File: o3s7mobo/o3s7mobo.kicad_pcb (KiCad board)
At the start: 2 copper layers, 330 x 216 mm, 0 parts

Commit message: Initial placement of 0.1" headers
Obviously far from finalized, but I wanted to start with what I could easily add.
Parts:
- added REF**: PinHeader_2x05_P2.54mm_Vertical, Connector_PinHeader_2.54mm:PinHeader_2x05_P2.54mm_Vertical, F.Cu at (256.0, 201.5)
- added REF**: PinHeader_2x20_P2.54mm_Vertical, Connector_PinHeader_2.54mm:PinHeader_2x20_P2.54mm_Vertical, F.Cu at (254.5, 186.5)
- added REF**: PinHeader_2x05_P2.54mm_Vertical, Connector_PinHeader_2.54mm:PinHeader_2x05_P2.54mm_Vertical, F.Cu at (275.0, 201.5)
- added REF**: PinHeader_2x13_P2.54mm_Vertical, Connector_PinHeader_2.54mm:PinHeader_2x13_P2.54mm_Vertical, F.Cu at (40.0, 37.0)
- added REF**: PinHeader_2x05_P2.54mm_Vertical, Connector_PinHeader_2.54mm:PinHeader_2x05_P2.54mm_Vertical, F.Cu at (60.5, 23.0)
- added REF**: PinHeader_2x05_P2.54mm_Vertical, Connector_PinHeader_2.54mm:PinHeader_2x05_P2.54mm_Vertical, F.Cu at (41.5, 23.0)
- added REF**: PinHeader_2x09_P2.54mm_Vertical, Connector_PinHeader_2.54mm:PinHeader_2x09_P2.54mm_Vertical, F.Cu at (40.5, 50.0)
- added REF**: PinHeader_2x08_P2.54mm_Vertical, Connector_PinHeader_2.54mm:PinHeader_2x08_P2.54mm_Vertical, F.Cu at (294.5, 201.5)
- added REF**: PinHeader_2x17_P2.54mm_Vertical, Connector_PinHeader_2.54mm:PinHeader_2x17_P2.54mm_Vertical, F.Cu at (254.5, 162.0)
- added REF**: PinHeader_2x20_P2.54mm_Vertical, Connector_PinHeader_2.54mm:PinHeader_2x20_P2.54mm_Vertical, F.Cu at (254.5, 176.0)

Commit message: Fix floppy connector, place labels of headers
I still need to finalize the front panel design, but I'm probably going to have something more standard.
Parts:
- removed REF**: PinHeader_2x17_P2.54mm_Vertical, Connector_PinHeader_2.54mm:PinHeader_2x17_P2.54mm_Vertical
- added FD0/1: PinHeader_2x16_P2.54mm_Vertical, Connector_PinHeader_2.54mm:PinHeader_2x16_P2.54mm_Vertical, F.Cu at (255.0, 166.0)
- renumbered REF** to ATXFORM, REF** to FPANEL, REF** to IDE0, REF** to IDE1, REF** to LPT0, REF** to SERIAL0, REF** to SERIAL1, REF** to USB2_0, REF** to USB2_1

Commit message: Removed key pins on headers
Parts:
- removed IDE0: PinHeader_2x20_P2.54mm_Vertical, Connector_PinHeader_2.54mm:PinHeader_2x20_P2.54mm_Vertical
- added IDE2: PinHeader_2x20_P2.54mm_Vertical, Connector_PinHeader_2.54mm:PinHeader_2x20_P2.54mm_Vertical, F.Cu at (255.0, 182.5)
- moved IDE1 13.0 mm to (255.0, 173.5)
- moved FLOPPY 4.61 mm to (256.0, 161.5)
- renumbered FD0/1 to FLOPPY, LPT0 to PARALLEL1, SERIAL0 to SERIAL1, SERIAL1 to SERIAL2

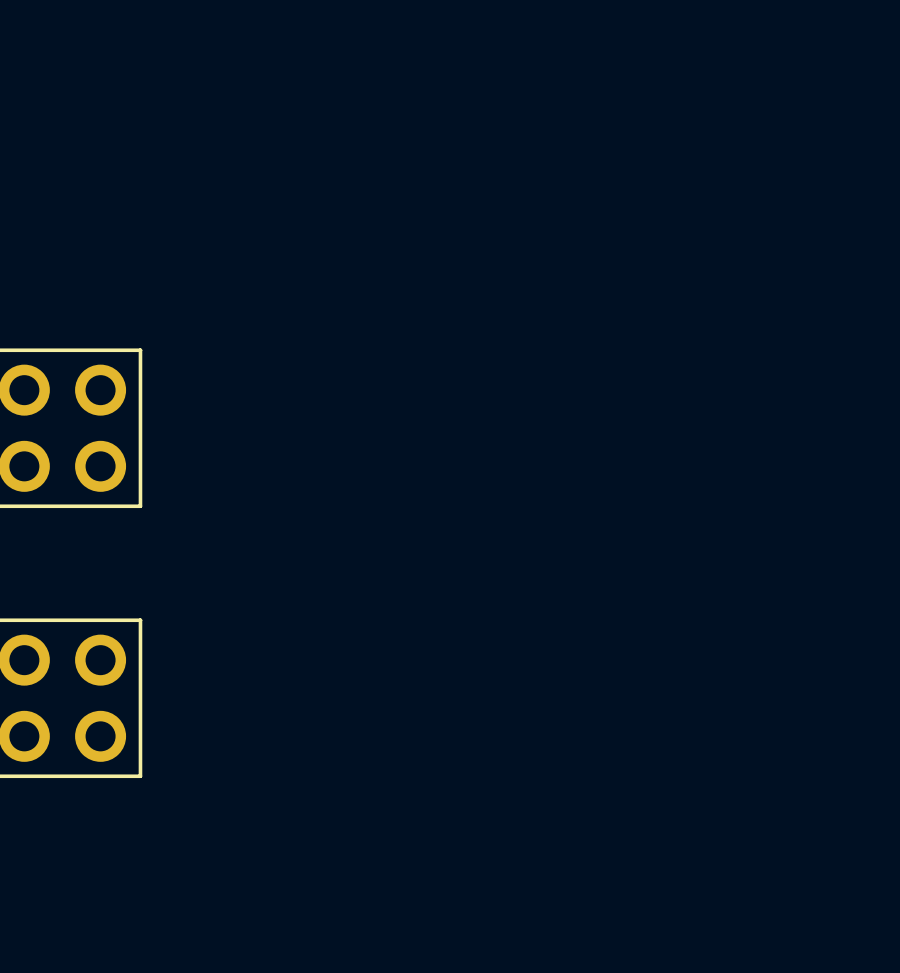
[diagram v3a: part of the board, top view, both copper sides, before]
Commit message: Added CMOS battery socket, minor bugfixing
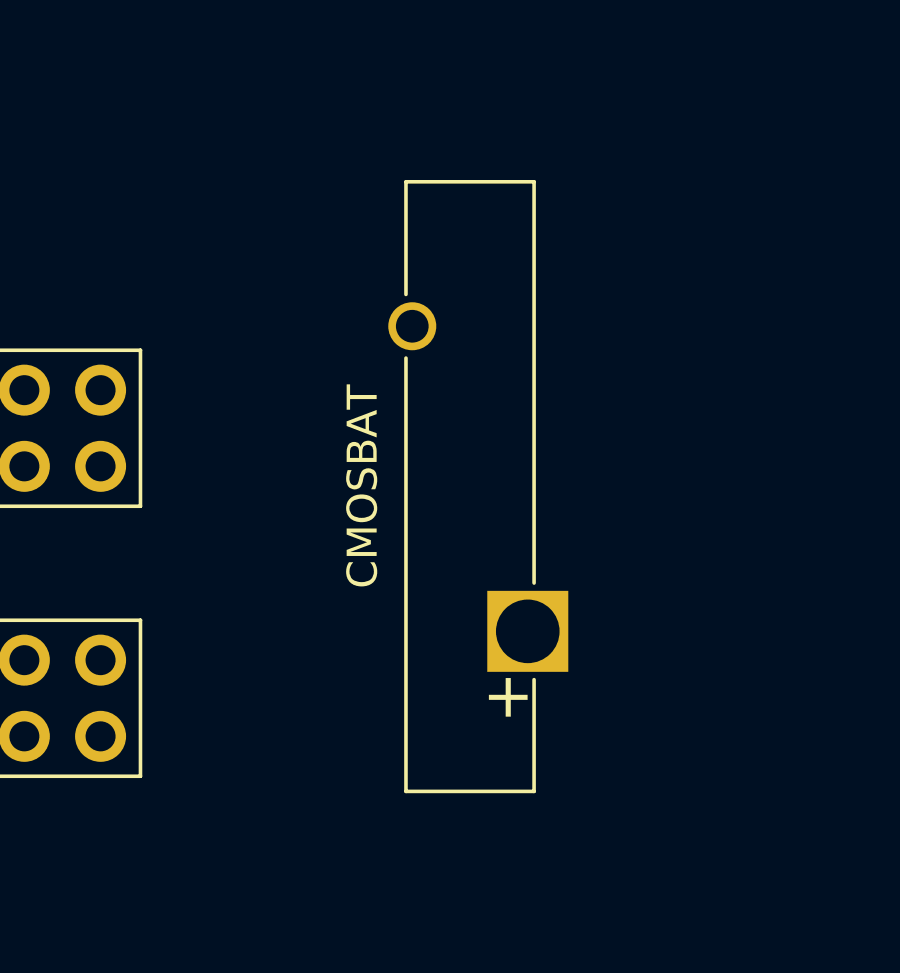
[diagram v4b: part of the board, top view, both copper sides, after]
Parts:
- added CMOSBAT: Battery_Panasonic_CR2032-VS1N_Vertical_CircularHoles, Battery:Battery_Panasonic_CR2032-VS1N_Vertical_CircularHoles, F.Cu at (317.5, 179.0)
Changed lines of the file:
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@@
     (tracks 0)
     (zones 0)
-    (modules 10)
+    (modules 11)
     (nets 1)
   )
@@
     (uvia_drill 0.1)
   )
+  (module Battery:Battery_Panasonic_CR2032-VS1N_Vertical_CircularHoles (layer F.Cu)
+    (at 317.5 179 90)
+    (descr "Panasonic CR-2032/VS1N battery, https://industrial.panasonic.com/cdbs/www-data/pdf2/AAA4000/AAA4000D140.pdf")
+    (tags "battery CR-2032 coin cell vertical")
+    (fp_text reference CMOSBAT (at 4.825 -5.5 90) (layer F.SilkS)
+      (effects (font (size 1 1) (thickness 0.15)))
+    )
+    (fp_text value Battery_Panasonic_CR2032-VS1N_Vertical_CircularHoles (at 4.825 2.5 90) (layer F.Fab)
+      (effects (font (size 1 1) (thickness 0.15)))
+    )
+    (fp_text user + (at -2.2 -0.7 90) (layer F.SilkS)
+      (effects (font (size 1.5 1.5) (thickness 0.15)))
+    )
+    (fp_text user %R (at 4.825 -2 270) (layer F.Fab)
+      (effects (font (size 1 1) (thickness 0.15)))
+    )
+    (fp_line (start -5.225 -3.95) (end 14.875 -3.95) (layer F.Fab) (width 0.1))
+    (fp_line (start 14.875 -3.95) (end 14.875 0.1) (layer F.Fab) (width 0.1))
+    (fp_line (start -5.225 -3.95) (end -5.225 0.1) (layer F.Fab) (width 0.1))
+    (fp_line (start -5.225 0.1) (end 14.875 0.1) (layer F.Fab) (width 0.1))
+    (fp_line (start -5.335 -4.06) (end 9.11 -4.06) (layer F.SilkS) (width 0.12))
+    (fp_line (start 11.23 -4.06) (end 14.985 -4.06) (layer F.SilkS) (width 0.12))
+    (fp_line (start 14.985 -4.06) (end 14.985 0.21) (layer F.SilkS) (width 0.12))
+    (fp_line (start -5.335 -4.06) (end -5.335 0.21) (layer F.SilkS) (width 0.12))
+    (fp_line (start -5.335 0.21) (end -1.61 0.21) (layer F.SilkS) (width 0.12))
+    (fp_line (start 1.61 0.21) (end 14.985 0.21) (layer F.SilkS) (width 0.12))
+    (fp_line (start -5.48 -4.78) (end -5.48 1.45) (layer F.CrtYd) (width 0.05))
+    (fp_line (start -5.48 1.45) (end 15.13 1.45) (layer F.CrtYd) (width 0.05))
+    (fp_line (start -5.48 -4.78) (end 15.13 -4.78) (layer F.CrtYd) (width 0.05))
+    (fp_line (start 15.13 -4.78) (end 15.13 1.45) (layer F.CrtYd) (width 0.05))
+    (pad 2 thru_hole circle (at 10.17 -3.85 90) (size 1.6 1.6) (drill 1.09) (layers *.Cu *.Mask))
+    (pad 1 thru_hole rect (at 0 0 180) (size 2.7 2.7) (drill 2.12) (layers *.Cu *.Mask))
+    (model ${KISYS3DMOD}/Battery.3dshapes/Battery_Panasonic_CR2032-VS1N_Vertical_CircularHoles.wrl
+      (at (xyz 0 0 0))
+      (scale (xyz 1 1 1))
+      (rotate (xyz 0 0 0))
+    )
+  )
   (module Connector_PinHeader_2.54mm:PinHeader_2x05_P2.54mm_Vertical (layer F.Cu)

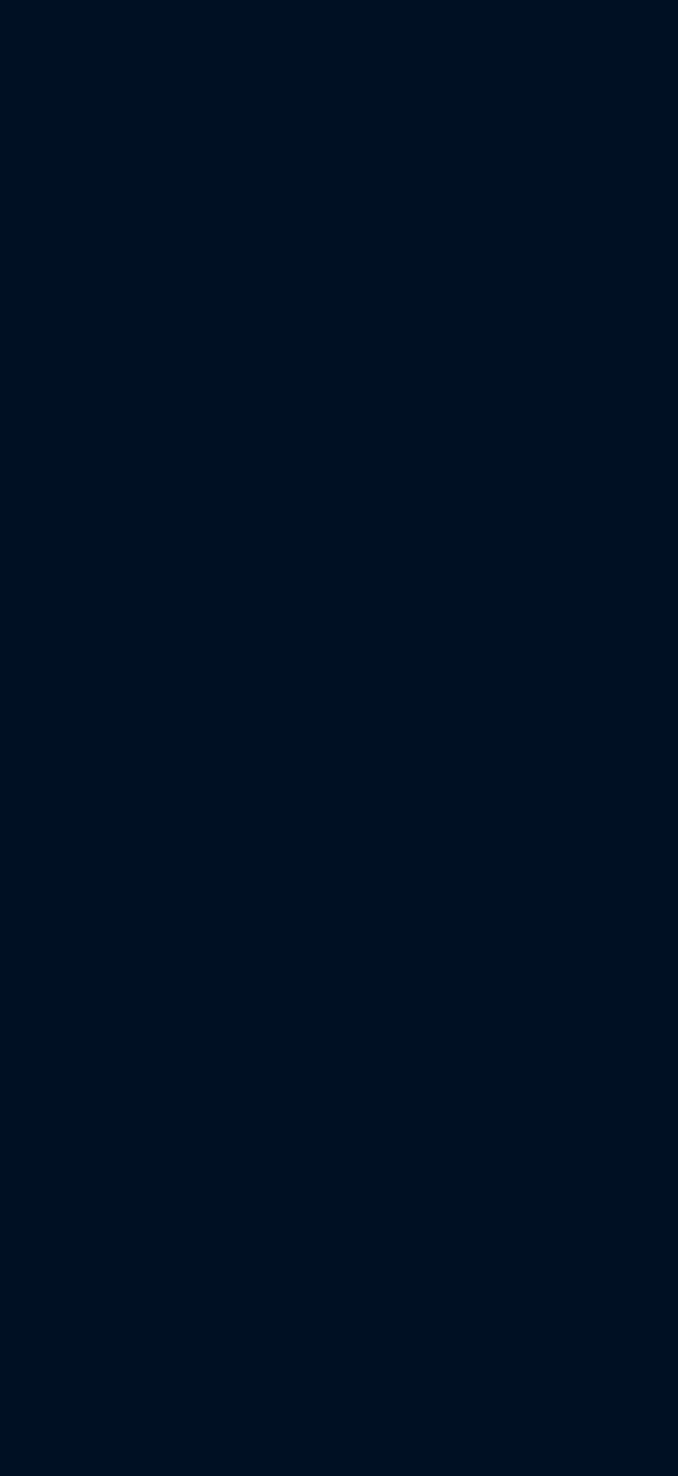
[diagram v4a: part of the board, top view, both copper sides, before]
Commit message: Added M1541 and M1543 BGA pads
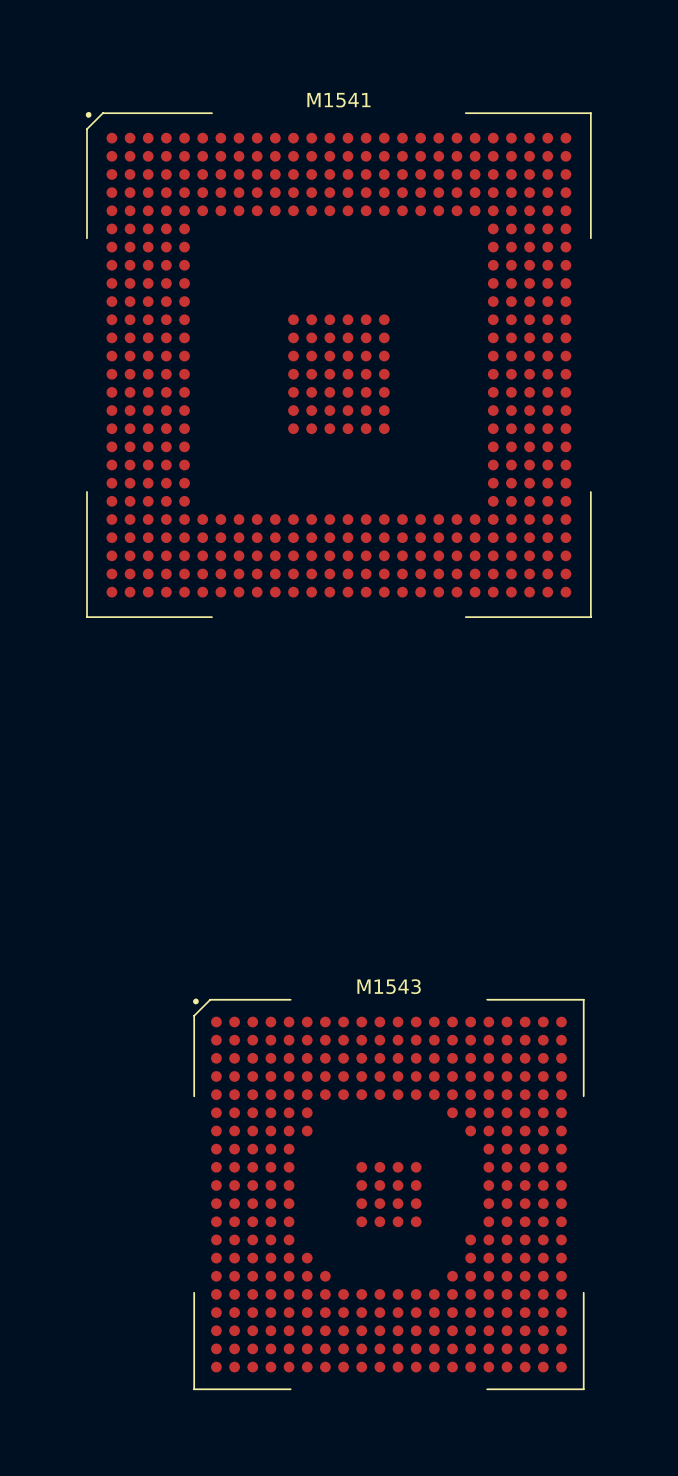
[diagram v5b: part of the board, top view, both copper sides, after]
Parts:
- added M1541: M1541, Downloaded:M1541, F.Cu at (171.0, 104.0)
- added M1543: M1543, Downloaded:M1543, F.Cu at (174.5, 162.0)

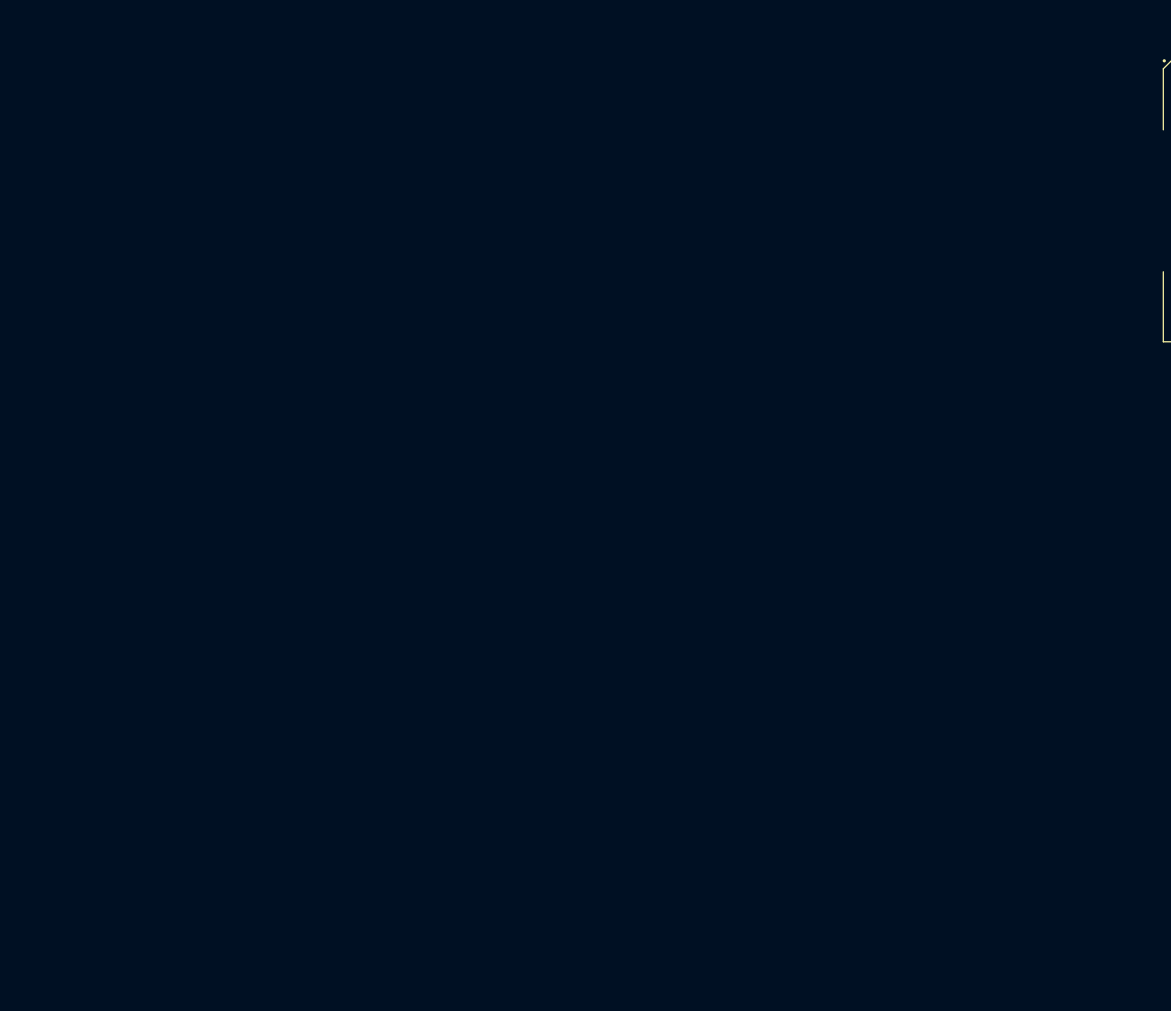
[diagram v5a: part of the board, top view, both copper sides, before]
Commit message: Created and initially placed PCI and ISA slots
The placement NEEDS to be verified on PCI and ISA slots. There's no way I got it 100% right by blind shooting.
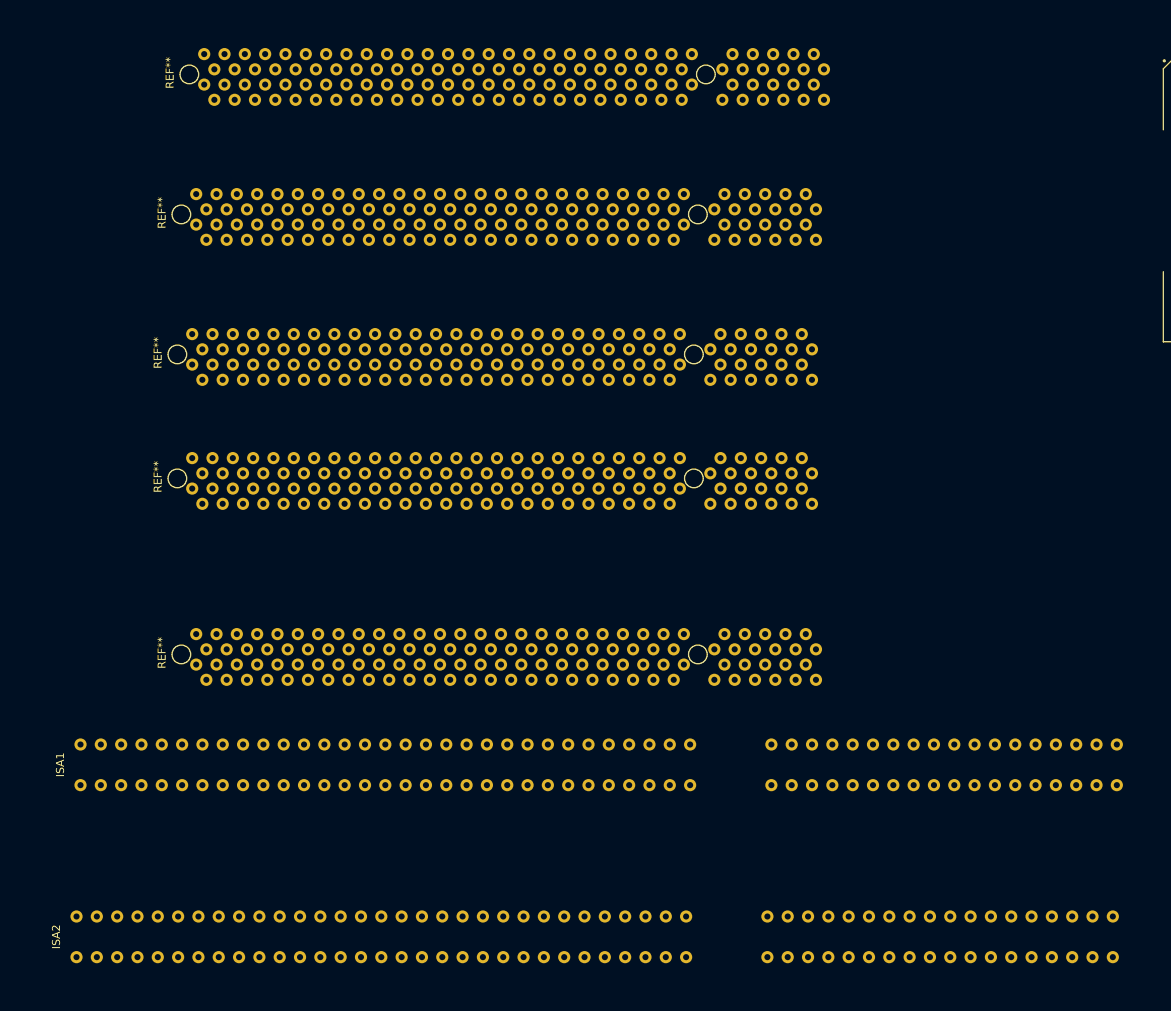
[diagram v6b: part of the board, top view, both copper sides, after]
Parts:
- added ISA1: ISA, Downloaded:ISA, F.Cu at (32.0, 174.5)
- added ISA2: ISA, Downloaded:ISA, F.Cu at (31.5, 196.0)
- added REF**: PCI, Downloaded:PCI, F.Cu at (50.0, 93.0)
- added REF**: PCI, Downloaded:PCI, F.Cu at (49.0, 110.5)
- added REF**: PCI, Downloaded:PCI, F.Cu at (48.5, 128.0)
- added REF**: PCI, Downloaded:PCI, F.Cu at (48.5, 143.5)
- added REF**: PCI, Downloaded:PCI, F.Cu at (49.0, 165.5)

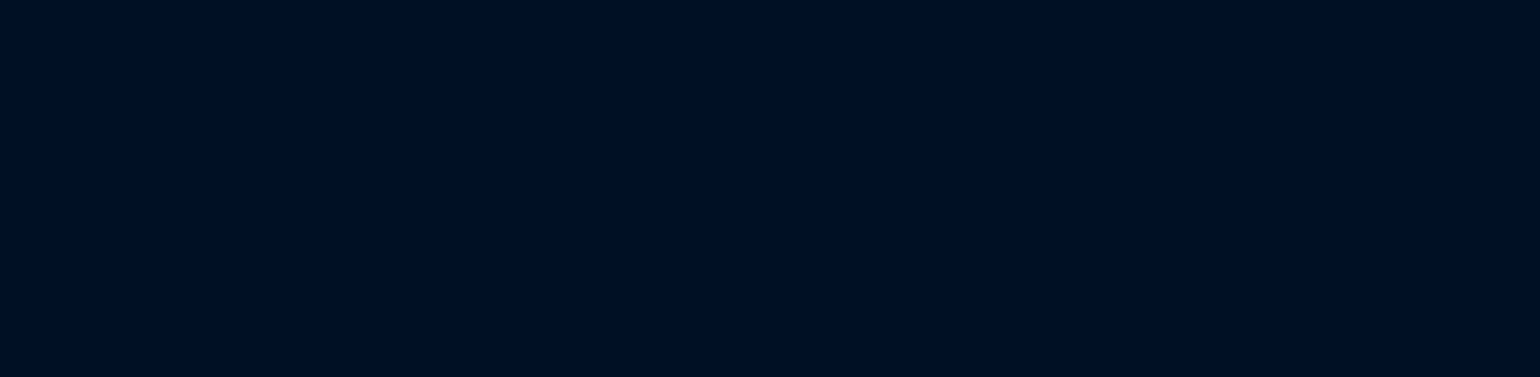
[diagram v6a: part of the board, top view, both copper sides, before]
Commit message: AGP slot added
I guess this now officially makes it a Super Socket 7 motherboard!
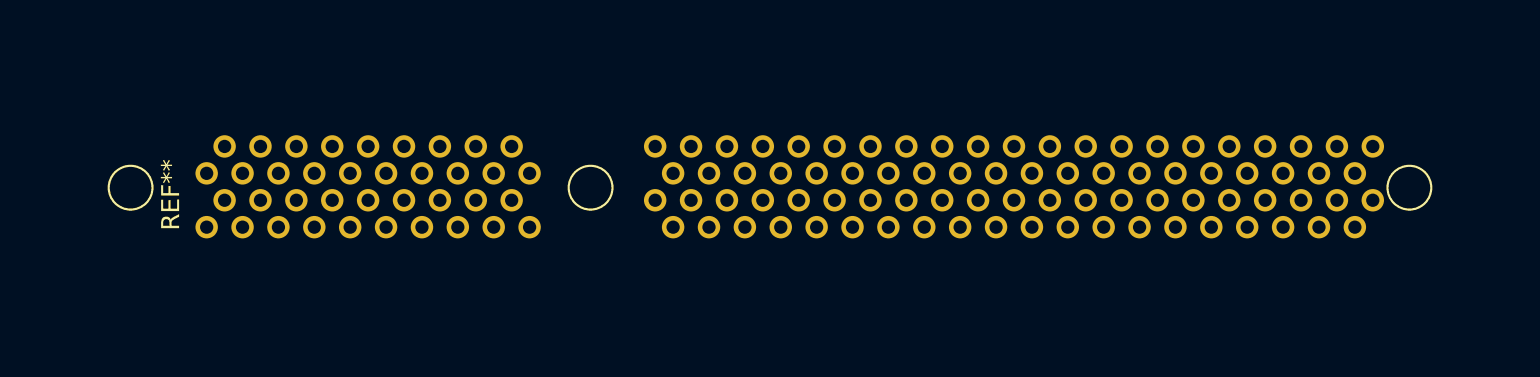
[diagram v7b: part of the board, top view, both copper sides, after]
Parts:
- added REF**: AGP, Downloaded:AGP, F.Cu at (74.5, 71.0)

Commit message: Added mounting holes
Now I gotta align the card slots.
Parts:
- added ?: MountingHole_3.5mm_Pad_Via, MountingHole:MountingHole_3.5mm_Pad_Via, F.Cu at (322.5, 204.5)
- added ?: MountingHole_3.5mm_Pad_Via, MountingHole:MountingHole_3.5mm_Pad_Via, F.Cu at (322.5, 75.0)
- added ?: MountingHole_3.5mm_Pad_Via, MountingHole:MountingHole_3.5mm_Pad_Via, F.Cu at (165.0, 75.0)
- added ?: MountingHole_3.5mm_Pad_Via, MountingHole:MountingHole_3.5mm_Pad_Via, F.Cu at (152.4, 3.96)
- added ?: MountingHole_3.5mm_Pad_Via, MountingHole:MountingHole_3.5mm_Pad_Via, F.Cu at (10.1, 3.91)
- added ?: MountingHole_3.5mm_Pad_Via, MountingHole:MountingHole_3.5mm_Pad_Via, F.Cu at (10.1, 75.0)
- added ?: MountingHole_3.5mm_Pad_Via, MountingHole:MountingHole_3.5mm_Pad_Via, F.Cu at (10.1, 120.8)
- added ?: MountingHole_3.5mm_Pad_Via, MountingHole:MountingHole_3.5mm_Pad_Via, F.Cu at (10.1, 199.5)
- added ?: MountingHole_3.5mm_Pad_Via, MountingHole:MountingHole_3.5mm_Pad_Via, F.Cu at (165.1, 199.5)
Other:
- board size 330 x 216 mm -> 330 x 217 mm
